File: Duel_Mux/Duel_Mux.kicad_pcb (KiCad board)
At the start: 2 copper layers, 100 x 68 mm, 7 parts, among them J1 Conn_01x08_Pin, J2 Conn_01x02_Pin, J3 2xRJ_45, J4 Conn_01x08_Pin, J5 Conn_01x03_Pin, U1 ADG406BNZ, U2 ADG406BNZ

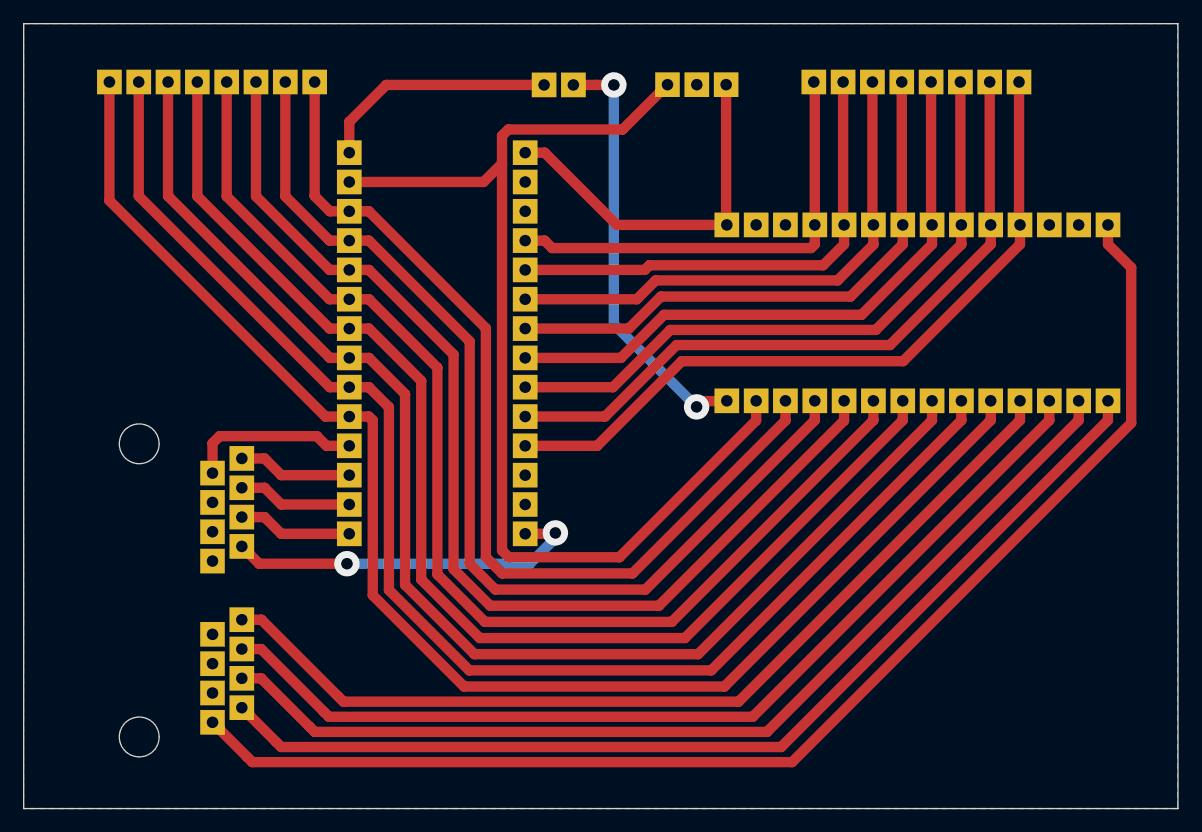
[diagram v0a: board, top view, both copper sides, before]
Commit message: Push update demodulation error test and updated duel mux
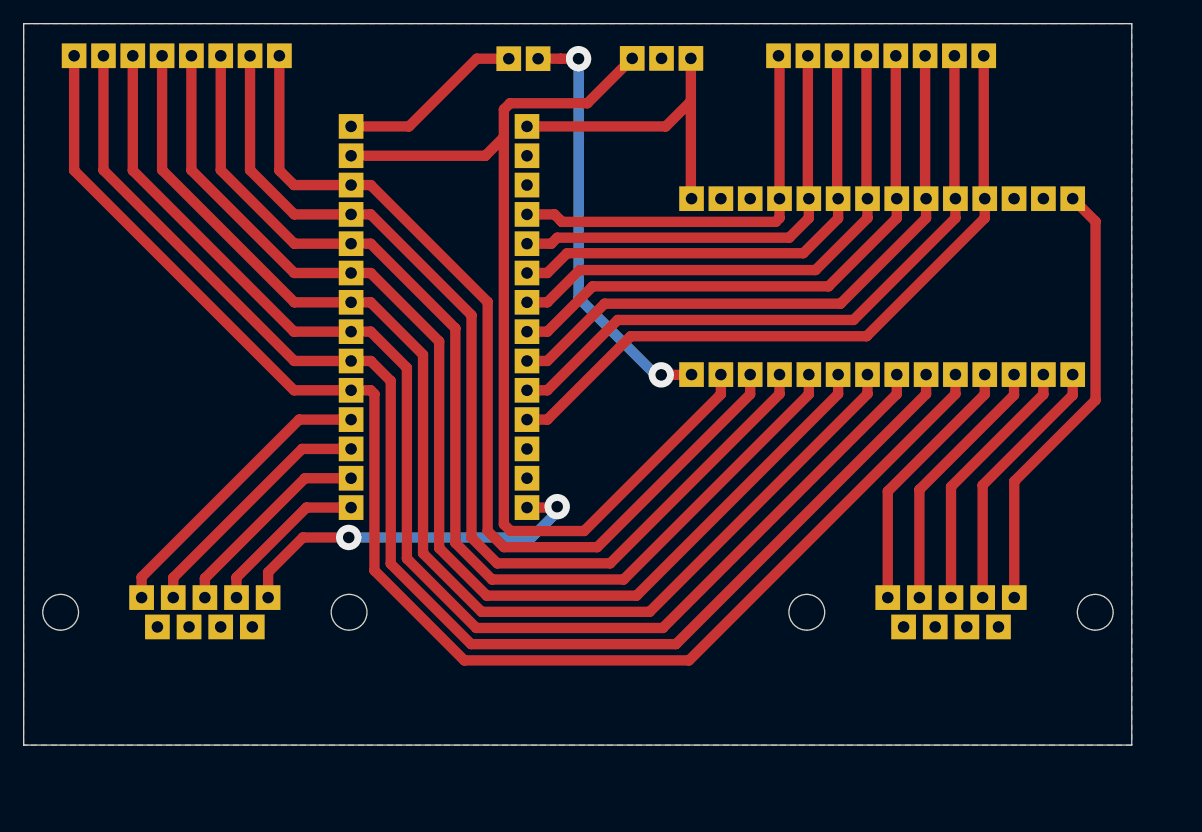
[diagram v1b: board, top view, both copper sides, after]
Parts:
- added J6: DB-9_Female, DB-9_Female:DB-9_Female, B.Cu at (80.3, 62.7)
- J5: renamed from J3; value 2xRJ_45 -> DB-9_Female; footprint TE_2xRJ45:TE_2xRJ45 -> DB-9_Female:DB-9_Female
- moved J5 14.6 mm to (15.7, 62.7), turned to 0 degrees
- moved J4 3.81 mm to (4.37, 2.78)
- moved J3 3.81 mm to (44.6, 3.04)
- moved J1 3.81 mm to (83.2, 2.78)
- moved J2 3.81 mm to (52.7, 3.01)
- moved U2 3.81 mm to (57.9, 15.2)
- moved U1 2.28 mm to (43.6, 8.90)
- renumbered J5 to J2, J2 to J3
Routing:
- net /A3_1: track 111.2 -> 38.3 mm
- net /A2_1: track 89.9 -> 22.6 mm
- net /A1_1: track 87.3 -> 22.6 mm
- net /A0_1: track 84.7 -> 22.7 mm
- net /EN_1: track 82.1 -> 22.8 mm
- net /A0_2: track 9.91 -> 22.4 mm
- net /EN_2: track 15.6 -> 26.2 mm
- net /A1_2: track 9.91 -> 18.6 mm
- net /-12V: track 94.9 -> 88.4 mm
- net /+12V: track 32.2 -> 27.3 mm
- net /A2_2: track 9.91 -> 14.8 mm
- net /D2: track 20.9 -> 16.1 mm
- net /CH15: track 42.6 -> 39.4 mm
- net /CH14: track 46.3 -> 43.0 mm
- net /CH13: track 49.8 -> 46.6 mm
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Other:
- board size 100 x 68 mm -> 96 x 62.5 mm
